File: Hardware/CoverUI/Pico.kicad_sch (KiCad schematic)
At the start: 2 parts, among them J2 Conn_01x06_Male, U1 Raspberry-Pico

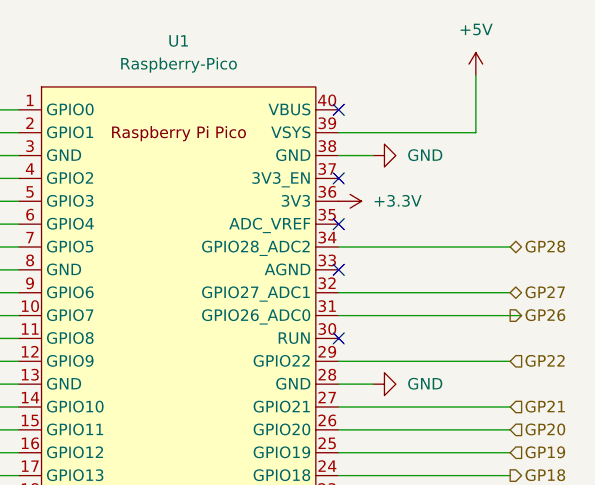
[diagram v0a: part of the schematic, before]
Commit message: fix(ui): connect 3.3V to 3V3
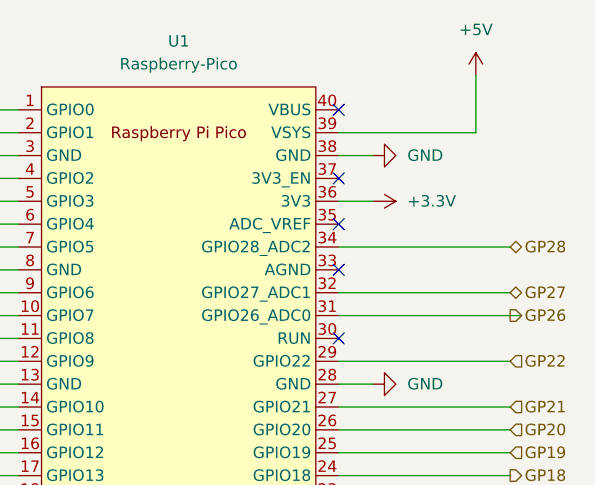
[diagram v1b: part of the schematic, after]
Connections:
- net +3V3 renamed +3.3V
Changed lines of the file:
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@@
+    (stroke (width 0) (type default) (color 0 0 0 0))
+  )
+  (wire (pts (xy 160.02 76.2) (xy 156.21 76.2))
     (stroke (width 0) (type default) (color 0 0 0 0))
   )
@@
     (pin "1")
   )
-  (symbol (lib_id "power:+3.3V") (at 156.21 76.2 270) (unit 1)
-    (in_bom yes) (on_board yes) (fields_autoplaced)
-    (property "Reference" "#PWR0101" (id 0) (at 152.4 76.2 0)
-      (effects (font (size 1.27 1.27)) hide)
-    )
-    (property "Value" "+3.3V" (id 1) (at 160.02 76.1999 90)
+  (symbol (lib_id "power:GND") (at 116.84 71.12 270) (unit 1)
+    (in_bom yes) (on_board yes) (fields_autoplaced)
+    (property "Reference" "#PWR0120" (id 0) (at 110.49 71.12 0)
+      (effects (font (size 1.27 1.27)) hide)
+    )
+    (property "Value" "GND" (id 1) (at 113.03 71.1201 90)
+      (effects (font (size 1.27 1.27)) (justify right))
+    )
+    (property "Footprint" "" (id 2) (at 116.84 71.12 0)
+      (effects (font (size 1.27 1.27)) hide)
+    )
+    (property "Datasheet" "" (id 3) (at 116.84 71.12 0)
+      (effects (font (size 1.27 1.27)) hide)
+    )
+    (pin "1")
+  )
+  (symbol (lib_id "power:GND") (at 116.84 109.22 270) (unit 1)
+    (in_bom yes) (on_board yes) (fields_autoplaced)
+    (property "Reference" "#PWR0123" (id 0) (at 110.49 109.22 0)
+      (effects (font (size 1.27 1.27)) hide)
+    )
+    (property "Value" "GND" (id 1) (at 113.03 109.2201 90)
+      (effects (font (size 1.27 1.27)) (justify right))
+    )
+    (property "Footprint" "" (id 2) (at 116.84 109.22 0)
+      (effects (font (size 1.27 1.27)) hide)
+    )
+    (property "Datasheet" "" (id 3) (at 116.84 109.22 0)
+      (effects (font (size 1.27 1.27)) hide)
+    )
+    (pin "1")
+  )
+  (symbol (lib_id "power:+3.3V") (at 160.02 76.2 270) (unit 1)
+    (in_bom yes) (on_board yes) (fields_autoplaced)
+    (property "Reference" "#PWR0105" (id 0) (at 156.21 76.2 0)
+      (effects (font (size 1.27 1.27)) hide)
+    )
+    (property "Value" "+3.3V" (id 1) (at 163.83 76.1999 90)
       (effects (font (size 1.27 1.27)) (justify left))
     )
-    (property "Footprint" "" (id 2) (at 156.21 76.2 0)
-      (effects (font (size 1.27 1.27)) hide)
-    )
-    (property "Datasheet" "" (id 3) (at 156.21 76.2 0)
-      (effects (font (size 1.27 1.27)) hide)
-    )
-    (pin "1")
-  )
-  (symbol (lib_id "power:GND") (at 116.84 71.12 270) (unit 1)
-    (in_bom yes) (on_board yes) (fields_autoplaced)
-    (property "Reference" "#PWR0120" (id 0) (at 110.49 71.12 0)
-      (effects (font (size 1.27 1.27)) hide)
-    )
-    (property "Value" "GND" (id 1) (at 113.03 71.1201 90)
-      (effects (font (size 1.27 1.27)) (justify right))
-    )
-    (property "Footprint" "" (id 2) (at 116.84 71.12 0)
-      (effects (font (size 1.27 1.27)) hide)
-    )
-    (property "Datasheet" "" (id 3) (at 116.84 71.12 0)
-      (effects (font (size 1.27 1.27)) hide)
-    )
-    (pin "1")
-  )
-  (symbol (lib_id "power:GND") (at 116.84 109.22 270) (unit 1)
-    (in_bom yes) (on_board yes) (fields_autoplaced)
-    (property "Reference" "#PWR0123" (id 0) (at 110.49 109.22 0)
-      (effects (font (size 1.27 1.27)) hide)
-    )
-    (property "Value" "GND" (id 1) (at 113.03 109.2201 90)
-      (effects (font (size 1.27 1.27)) (justify right))
-    )
-    (property "Footprint" "" (id 2) (at 116.84 109.22 0)
-      (effects (font (size 1.27 1.27)) hide)
-    )
-    (property "Datasheet" "" (id 3) (at 116.84 109.22 0)
-      (effects (font (size 1.27 1.27)) hide)
-    )
+    (property "Footprint" "" (id 2) (at 160.02 76.2 0)
+      (effects (font (size 1.27 1.27)) hide)
+    )
+    (property "Datasheet" "" (id 3) (at 160.02 76.2 0)
+      (effects (font (size 1.27 1.27)) hide)
+    )
